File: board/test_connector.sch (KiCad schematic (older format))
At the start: 5 parts, among them P1 test_connector

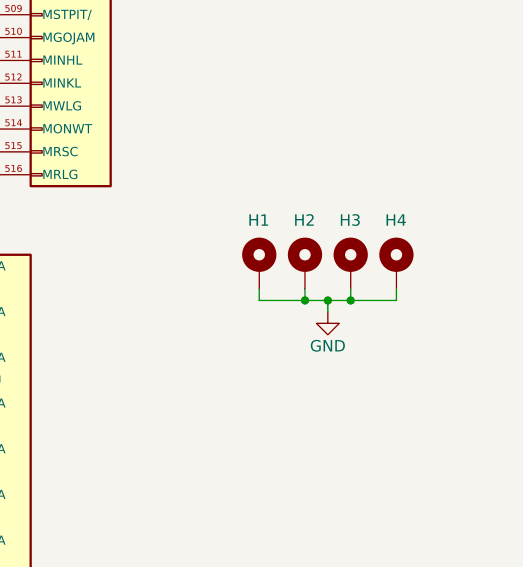
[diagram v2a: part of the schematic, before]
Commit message: Redid the mechanical outline of the board; further development/layout
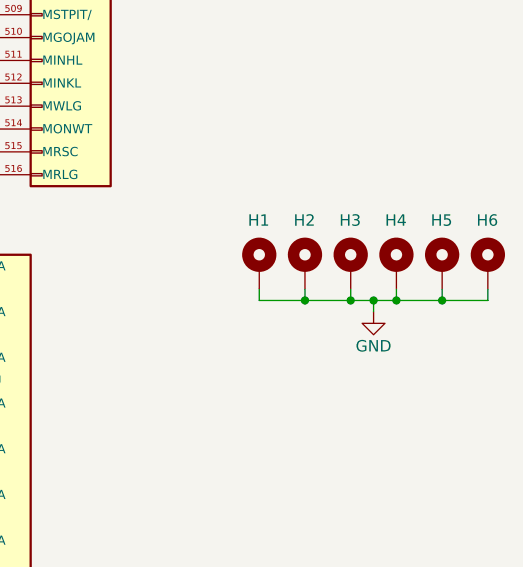
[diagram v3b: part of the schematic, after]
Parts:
- added H5, H6: MountingHole_Pad, agc_monitor:MountingHole_ANSI_4, symbol Mechanical:MountingHole_Pad
- H1, H2, H3, H4: footprint agc_monitor:MountingHole_1004579 -> agc_monitor:MountingHole_ANSI_4
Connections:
- net GND: now also H5.1, H6.1
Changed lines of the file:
@@
 F 0 "H1" H 8950 4050 50  0000 L CNN
 F 1 "MountingHole_Pad" H 9100 3810 50  0001 L CNN
-F 2 "agc_monitor:MountingHole_1004579" H 9000 3850 50  0001 C CNN
+F 2 "agc_monitor:MountingHole_ANSI_4" H 9000 3850 50  0001 C CNN
 F 3 "~" H 9000 3850 50  0001 C CNN
 	1    9000 3850
@@
 L power:GND #PWR0160
 U 1 1 5C7A2406
-P 9300 4050
-F 0 "#PWR0160" H 9300 3800 50  0001 C CNN
-F 1 "GND" H 9300 3900 50  0000 C CNN
-F 2 "" H 9300 4050 50  0001 C CNN
-F 3 "" H 9300 4050 50  0001 C CNN
-	1    9300 4050
+P 9500 4050
+F 0 "#PWR0160" H 9500 3800 50  0001 C CNN
+F 1 "GND" H 9500 3900 50  0000 C CNN
+F 2 "" H 9500 4050 50  0001 C CNN
+F 3 "" H 9500 4050 50  0001 C CNN
+	1    9500 4050
 	1    0    0    -1
 $EndComp
@@
 F 0 "H2" H 9150 4050 50  0000 L CNN
 F 1 "MountingHole_Pad" H 9300 3810 50  0001 L CNN
-F 2 "agc_monitor:MountingHole_1004579" H 9200 3850 50  0001 C CNN
+F 2 "agc_monitor:MountingHole_ANSI_4" H 9200 3850 50  0001 C CNN
 F 3 "~" H 9200 3850 50  0001 C CNN
 	1    9200 3850
@@
 F 0 "H3" H 9350 4050 50  0000 L CNN
 F 1 "MountingHole_Pad" H 9500 3810 50  0001 L CNN
-F 2 "agc_monitor:MountingHole_1004579" H 9400 3850 50  0001 C CNN
+F 2 "agc_monitor:MountingHole_ANSI_4" H 9400 3850 50  0001 C CNN
 F 3 "~" H 9400 3850 50  0001 C CNN
 	1    9400 3850
@@
 F 0 "H4" H 9550 4050 50  0000 L CNN
 F 1 "MountingHole_Pad" H 9700 3810 50  0001 L CNN
-F 2 "agc_monitor:MountingHole_1004579" H 9600 3850 50  0001 C CNN
+F 2 "agc_monitor:MountingHole_ANSI_4" H 9600 3850 50  0001 C CNN
 F 3 "~" H 9600 3850 50  0001 C CNN
 	1    9600 3850
@@
 	9000 4000 9200 4000
 Wire Wire Line
-	9300 4000 9300 4050
-Wire Wire Line
-	9300 4000 9400 4000
+	9500 4000 9500 4050
 Wire Wire Line
 	9600 4000 9600 3950
-Connection ~ 9300 4000
 Wire Wire Line
 	9400 3950 9400 4000
-Connection ~ 9400 4000
 Wire Wire Line
-	9400 4000 9600 4000
+	9400 4000 9500 4000
 Wire Wire Line
 	9200 3950 9200 4000
-Connection ~ 9200 4000
-Wire Wire Line
-	9200 4000 9300 4000
 $Comp
 L agc_monitor:+3V3_IO #PWR0135
@@
 Wire Wire Line
 	4650 4050 5100 4050
+$Comp
+L Mechanical:MountingHole_Pad H5
+U 1 1 5C8E6EAB
+P 9800 3850
+F 0 "H5" H 9750 4050 50  0000 L CNN
+F 1 "MountingHole_Pad" H 9900 3810 50  0001 L CNN
+F 2 "agc_monitor:MountingHole_ANSI_4" H 9800 3850 50  0001 C CNN
+F 3 "~" H 9800 3850 50  0001 C CNN
+	1    9800 3850
+	1    0    0    -1
+$EndComp
+$Comp
+L Mechanical:MountingHole_Pad H6
+U 1 1 5C8E6EB1
+P 10000 3850
+F 0 "H6" H 9950 4050 50  0000 L CNN
+F 1 "MountingHole_Pad" H 10100 3810 50  0001 L CNN
+F 2 "agc_monitor:MountingHole_ANSI_4" H 10000 3850 50  0001 C CNN
+F 3 "~" H 10000 3850 50  0001 C CNN
+	1    10000 3850
+	1    0    0    -1
+$EndComp
+Wire Wire Line
+	9200 4000 9400 4000
+Connection ~ 9200 4000
+Connection ~ 9400 4000
+Wire Wire Line
+	9600 4000 9800 4000
+Wire Wire Line
+	9800 4000 9800 3950
+Connection ~ 9600 4000
+Wire Wire Line
+	9800 4000 10000 4000
+Wire Wire Line
+	10000 4000 10000 3950
+Connection ~ 9800 4000
+Connection ~ 9500 4000
+Wire Wire Line
+	9500 4000 9600 4000
 $EndSCHEMATC
